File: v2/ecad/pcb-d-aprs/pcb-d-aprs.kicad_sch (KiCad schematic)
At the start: 96 parts, among them Q1 BC847 (PTT2, spare), Q2 BC847 (PTT to the module), Q3 2N7002 (EMCON inhibit in Q2 e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, Q4 BC857 (TR mirror from RADIO_P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, U1 TPS61089 boost 7.6 V / 2 A, U2 DNP bench: DMR858M 5 W UHF mo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, U3 AP2112K-3.3 digital, U4 AP2112K-3.3 analog, U5 STM32F302CBT6 128 KB (AIOC fi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, U6 USBLC6-2SC6, Y1 8MHz 20pF 5032

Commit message: feat(pcb-a,pcb-d): A20 and D6 routed and finished on the laptop [MESHSAT-795]
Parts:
- removed C1, C2: 22p NP0, Capacitor_SMD:C_0603_1608Metric, symbol Device:C
- removed C11: 4.7n NP0, Capacitor_SMD:C_0603_1608Metric, symbol Device:C
- removed C12, C15, C16: 100n, Capacitor_SMD:C_0603_1608Metric, symbol Device:C
- removed C31, C4, C5, C6: 4.7u, Capacitor_SMD:C_0603_1608Metric, symbol Device:C
- removed D2: red, LED_SMD:LED_0603_1608Metric, symbol Device:LED
- removed FB2: 600R@100MHz, Inductor_SMD:L_0603_1608Metric, symbol Device:FerriteBead
- removed J_SWD1: SWD/DFU 1.27 mm: BOOT0 SWO NRST SWDIO GND SWCLK 3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, Connector_PinHeader_1.27mm:PinHeader_1x07_P1.27mm_Vertical, symbol Connector_Generic:Conn_01x07
- removed R1, R18, R19: 1.5k, Resistor_SMD:R_0603_1608Metric, symbol Device:R
- removed R14, R16, R5: 5.1k, Resistor_SMD:R_0603_1608Metric, symbol Device:R
- removed R17: 100R, Resistor_SMD:R_0603_1608Metric, symbol Device:R
- removed R22: DNP 100R (mirror now via Q4), Resistor_SMD:R_0603_1608Metric, symbol Device:R
- removed U3: AP2112K-3.3 digital, Package_TO_SOT_SMD:SOT-23-5, symbol Regulator_Linear:AP2112K-3.3
- removed U4: AP2112K-3.3 analog, Package_TO_SOT_SMD:SOT-23-5, symbol Regulator_Linear:AP2112K-3.3
- removed U5: STM32F302CBT6 128 KB (AIOC firmware 1.4.1 is 128,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, Package_QFP:LQFP-48_7x7mm_P0.5mm, symbol MCU_ST_STM32F3:STM32F302CBTx
- removed U6: USBLC6-2SC6, Package_TO_SOT_SMD:SOT-23-6, symbol Power_Protection:USBLC6-2SC6
- removed Y1: 8MHz 20pF 5032, Crystal:Crystal_SMD_5032-2Pin_5.0x3.2mm, symbol Device:Crystal
- added C33, C35, C36, C38, C39: 100n, Capacitor_SMD:C_0603_1608Metric, symbol Device:C
- added C34: 10u, Capacitor_SMD:C_1210_3225Metric, symbol Device:C
- added C37: 4.7u, Capacitor_SMD:C_0603_1608Metric, symbol Device:C
- added J_UART1: DMR858M host-upgrade UART (bench, 3.3 V, 100R in 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, Connector_PinHeader_2.54mm:PinHeader_1x03_P2.54mm_Vertical, symbol Connector_Generic:Conn_01x03
- added TP13: MCLK, TestPoint:TestPoint_Pad_D1.5mm, symbol Connector:TestPoint
- added TP14: +3V3_AB, TestPoint:TestPoint_Pad_D1.5mm, symbol Connector:TestPoint
- added TP15: I2S_BCLK, TestPoint:TestPoint_Pad_D1.5mm, symbol Connector:TestPoint
- added U5: WM8960 audio codec QFN-32 (pins per datasheet tab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, Package_DFN_QFN:QFN-32-1EP_5x5mm_P0.5mm_EP3.1x3.1mm, symbol Connector_Generic:Conn_02x17_Odd_Even
- added U7: PCA9536 4-bit I2C expander 0x41: 0 PTT, 1 PTT2 (s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, Package_SO:SOIC-8_3.9x4.9mm_P1.27mm, symbol Interface_Expansion:PCA9536D
- added X1: 24 MHz 3.3 V oscillator 3225 (ASE-24.000MHZ-LC-T 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, Oscillator:Oscillator_SMD_Abracon_ASE-4Pin_3.2x2.5mm, symbol Oscillator:ASE-xxxMHz
- D1: value green -> green status (U7 bit 3 sinks)
- J_HARN1: value harness to PCB-A J_MEZZ1 (IDC 2x8); UART pair and PCB-A 3V3 unused -> harness to PCB-A J_MEZZ1 (IDC 2x8): I2S, I2C, the gated 3.3 V from B13, PTT lines
- R15: value 100R -> 1k
- R3: value 100R -> 100k
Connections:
- net ADC_BIAS is gone; now on net GND: R3.2
- net BIAS_NODE is gone; now on net SPKEN: R3.1
- net LDO_A is gone; now on net +3V3_AB: FB1.1
- net LED_R is gone; now on net LED_A: R15.2
- net +3.3VA: now also C33.1, C34.1, U5.21 (Pin_21), U5.26 (Pin_26), U5.32 (Pin_32)
- net +3V3: now also J_HARN1.12 (Pin_12); no longer C18.1, C7.1, C8.1
- net AFOUT: now also U5.31 (Pin_31)
- net GND: now also J_HARN1.8 (Pin_8), C33.2, C34.2, C35.2, C36.2, C37.2, C38.2, C39.2, J_UART1.1 (Pin_1), U5.20 (Pin_20), U5.24 (Pin_24), U5.28 (Pin_28), U5.33 (Pin_33), U5.9 (Pin_9), U7.4 (VSS), X1.2 (GND); no longer J_HARN1.9 (Pin_9)
- net LED_K: now also U7.7 (SDA); no longer R15.1
- net OUT1: now also U7.1 (IO0)
- net OUT2: now also U7.2 (IO1)
- net SPKEN: now also U7.3 (IO2); no longer J_HARN1.14 (Pin_14)
- net I2S_DOUT: now reaches J_HARN1.6 (Pin_6)
- net I2S_DOUT: now also U5.14 (Pin_14)
- net I2S_DIN: now reaches J_HARN1.7 (Pin_7)
- net I2S_DIN: now also U5.16 (Pin_16)
- net +5V_USB renamed +3V3_AB
- net +3V3_AB: now also C18.1, C7.1, C8.1, R15.1, C35.1, C36.1, C38.1, C39.1, TP14.1, U5.10 (Pin_10), U5.8 (Pin_8), U7.8 (VDD), X1.1 (EN), X1.4 (Vdd)
- net SPK_NODE renamed SPK_IN
- net SPK_IN: now also U5.4 (Pin_4)
- net USART_RX renamed UART_RX_H
- net UART_RX_H: now also J_UART1.2 (Pin_2)
- net USART_TX renamed UART_TX_H
- net UART_TX_H: now also J_UART1.3 (Pin_3)
- net USB_DM renamed I2S_LRCLK
- net I2S_LRCLK: now also U5.13 (Pin_13), U5.15 (Pin_15)
- net USB_DP renamed I2S_BCLK
- net I2S_BCLK: now also TP15.1, U5.12 (Pin_12)
- new net MCLK: TP13.1, U5.11 (Pin_11), X1.3 (OUT)
- new net SCL: J_HARN1.14 (Pin_14), U5.17 (Pin_17), U7.6 (SCL)
- new net SDA: J_HARN1.9 (Pin_9), U5.18 (Pin_18), U7.5 (IO3)
- new net VMID: C37.1, U5.27 (Pin_27)
- no-connect marks 30 -> 20
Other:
- note added: "AUDIO PATHS, PTT + TR MIRROR, UART, LED"
- note added: "D6 CORE: RAILS, WM8960 CODEC ON I2S + I2C, 24 MHz CLOCK, PCA9536 PTT EXPANDER, UART HEADER"
- note removed: "AIOC-DERIVED CORE: LDOs, STM32F302C8, CLOCK, SWD/DFU"
- note removed: "USB, AUDIO PATHS, PTT + TR MIRROR, UART, LEDS"

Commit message: feat(pcb-d): D7 routed and finished for the DMR858M V1.0 board [MESHSAT-804]
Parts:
- removed JP1: channel bit CH8 to GND (open = default), Jumper:SolderJumper-2_P1.3mm_Open_RoundedPad1.0x1.5mm, symbol Jumper:SolderJumper_2_Open
- removed JP2: channel bit CH4 to GND (open = default), Jumper:SolderJumper-2_P1.3mm_Open_RoundedPad1.0x1.5mm, symbol Jumper:SolderJumper_2_Open
- removed JP3: channel bit CH2 to GND (open = default), Jumper:SolderJumper-2_P1.3mm_Open_RoundedPad1.0x1.5mm, symbol Jumper:SolderJumper_2_Open
- removed JP4: channel bit CH1 to GND (open = default), Jumper:SolderJumper-2_P1.3mm_Open_RoundedPad1.0x1.5mm, symbol Jumper:SolderJumper_2_Open
- removed JP5: CS to GND = module sleep, Jumper:SolderJumper-2_P1.3mm_Open_RoundedPad1.0x1.5mm, symbol Jumper:SolderJumper_2_Open
- removed J_UART1: DMR858M host-upgrade UART (bench, 3.3 V, 100R in 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, Connector_PinHeader_2.54mm:PinHeader_1x03_P2.54mm_Vertical, symbol Connector_Generic:Conn_01x03
- removed U7: PCA9536 4-bit I2C expander 0x41: 0 PTT, 1 PTT2 (s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, Package_SO:SOIC-8_3.9x4.9mm_P1.27mm, symbol Interface_Expansion:PCA9536D
- added C40: 100n, Capacitor_SMD:C_0603_1608Metric, symbol Device:C
- added R42, R43, R44, R45, R46, R48: 1k, Resistor_SMD:R_0603_1608Metric, symbol Device:R
- added R47: 10k, Resistor_SMD:R_0603_1608Metric, symbol Device:R
- added R49, R50, R51, R52: 100k, Resistor_SMD:R_0603_1608Metric, symbol Device:R
- added U7: PCA9555PW 0x26: PTT, PTT2, LED, CS, COS in, chann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, Package_SO:TSSOP-24_4.4x7.8mm_P0.65mm, symbol Interface_Expansion:PCA9555PW
- added U8: SC16IS740IPW I2C-to-UART bridge 0x48, 24 MHz exte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, Package_SO:TSSOP-16_4.4x5mm_P0.65mm, symbol Connector_Generic:Conn_01x16
- R2: value 4.7k -> 47k
- R4: value 1.5k -> 1k
- TP6: value SPKEN -> RADIO_COS
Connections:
- net +3V3: no longer R36.2
- net +3V3_AB: now also R36.2, C40.1, R47.2, U7.2 (A1), U7.24 (VDD), U7.3 (A2), U8.1 (Pin_1), U8.2 (Pin_2), U8.3 (Pin_3), U8.8 (Pin_8)
- net CH1: now also R46.1
- net CH2: now also R45.1
- net CH4: now also R44.1
- net CH8: now also R43.1
- net CS: now also R48.2
- net GND: now also C40.2, R49.2, R50.2, R51.2, R52.2, U7.12 (VSS), U7.21 (A0), U8.11 (Pin_11), U8.9 (Pin_9)
- net LED_K: now also U7.6 (IO0_2)
- net MCLK: now also U8.15 (Pin_15)
- net OUT1: now also U7.4 (IO0_0)
- net OUT2: now also U7.5 (IO0_1)
- net SCL: now also U7.22 (SCL), U8.5 (Pin_5)
- net SDA: now also U7.23 (SDA), U8.6 (Pin_6)
- net SPKEN renamed RADIO_COS
- net RADIO_COS: now also R42.1
- net UART_RX_H renamed BR_RX
- net BR_RX: now also U8.13 (Pin_13)
- net UART_TX_H renamed BR_TX
- net BR_TX: now also U8.12 (Pin_12)
- new net BR_nRST: R47.1, U8.14 (Pin_14)
- new net CH1_IN: R46.2, R52.1, U7.13 (IO1_0)
- new net CH2_IN: R45.2, R51.1, U7.11 (IO0_7)
- new net CH4_IN: R44.2, R50.1, U7.10 (IO0_6)
- new net CH8_IN: R43.2, R49.1, U7.9 (IO0_5)
- new net CS_CTL: R48.1, U7.7 (IO0_3)
- new net RADIO_COS_IN: R42.2, U7.8 (IO0_4)
- no-connect marks 20 -> 32
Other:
- note added: "AUDIO PATHS, PTT + TR MIRROR, BRIDGE UART LINES, LED"
- note added: "D7 CORE: RAILS, WM8960 CODEC ON I2S + I2C, 24 MHz CLOCK, PCA9555 EXPANDER 0x26, SC16IS740 UART BRIDGE 0x48"
- note added: "DMR858M RADIO MODULE (V1.0 BOARD): CS PULL-UP AND CONTROL, KNOB CODE AND COS INTO THE EXPANDER"
- note removed: "AUDIO PATHS, PTT + TR MIRROR, UART, LED"
- note removed: "D6 CORE: RAILS, WM8960 CODEC ON I2S + I2C, 24 MHz CLOCK, PCA9536 PTT EXPANDER, UART HEADER"
- note removed: "DMR858M RADIO MODULE: CHANNEL JUMPERS, CS"

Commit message: feat(ecad): D8 routed clean and released (SA868 exciter, T/R relay, LPF, USB audio and control set), C7 generators (backer ring, RP2040 panel controller, PDi e-paper driver, Xenarc face, headset jacks), per-closure stub acceptance, plane-net fanout fixes [MESHSAT-830]
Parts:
- removed D1: green status (U7 bit 3 sinks), LED_SMD:LED_0603_1608Metric, symbol Device:LED
- removed Q1: BC847 (PTT2, spare), Package_TO_SOT_SMD:SOT-23, symbol Transistor_BJT:BC847
- removed Q2: BC847 (PTT to the module), Package_TO_SOT_SMD:SOT-23, symbol Transistor_BJT:BC847
- removed Q4: BC857 (TR mirror from RADIO_PTT), Package_TO_SOT_SMD:SOT-23, symbol Transistor_BJT:BC857
- removed U1: TPS61089 boost 7.6 V / 2 A, Package_DFN_QFN:Texas_VQFN-RNR0011A-11, symbol Regulator_Switching:TPS61089
- removed U2: DNP bench: DMR858M 5 W UHF module on 2 x 1x12 2.5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, meshsat:DMR858M, symbol Connector_Generic:Conn_02x12_Odd_Even
- removed U5: WM8960 audio codec QFN-32 (pins per datasheet tab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, Package_DFN_QFN:QFN-32-1EP_5x5mm_P0.5mm_EP3.1x3.1mm, symbol Connector_Generic:Conn_02x17_Odd_Even
- removed U7: PCA9555PW 0x26: PTT, PTT2, LED, CS, COS in, chann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, Package_SO:TSSOP-24_4.4x7.8mm_P0.65mm, symbol Interface_Expansion:PCA9555PW
- removed U8: SC16IS740IPW I2C-to-UART bridge 0x48, 24 MHz exte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, Package_SO:TSSOP-16_4.4x5mm_P0.65mm, symbol Connector_Generic:Conn_01x16
- removed X1: 24 MHz 3.3 V oscillator 3225 (ASE-24.000MHZ-LC-T 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, Oscillator:Oscillator_SMD_Abracon_ASE-4Pin_3.2x2.5mm, symbol Oscillator:ASE-xxxMHz
- added C1, C2, C5: 47u 6.3V X5R 1210, Capacitor_SMD:C_1210_3225Metric, symbol Device:C
- added C11, C15, C16, C4, C49, C50, C51, C52, C53, C54, C55, C56, C57, C6, C62, C63: 100n, Capacitor_SMD:C_0603_1608Metric, symbol Device:C
- added C12, C19, C31, C41, C42, C46, C47, C48: 1u, Capacitor_SMD:C_0603_1608Metric, symbol Device:C
- added C3: 10u, Capacitor_SMD:C_0805_2012Metric, symbol Device:C
- added C43: 100p NP0, Capacitor_SMD:C_0402_1005Metric, symbol Device:C
- added C44, C45: 1n NP0, Capacitor_SMD:C_0402_1005Metric, symbol Device:C
- added C58, C60: 22p 500V NP0 1206, Capacitor_SMD:C_1206_3216Metric, symbol Device:C
- added C59: 39p 500V NP0 1206, Capacitor_SMD:C_1206_3216Metric, symbol Device:C
- added C61: 4.7n, Capacitor_SMD:C_0402_1005Metric, symbol Device:C
- added D1: SMBJ5.0A, Diode_SMD:D_SMB, symbol Device:D_TVS
- added D2: 1N4148W coil flyback, Diode_SMD:D_SOD-123, symbol Diode:1N4148W
- added JP1: electret bias headset 1 (close for an electret mi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, Jumper:SolderJumper-2_P1.3mm_Open_RoundedPad1.0x1.5mm, symbol Jumper:SolderJumper_2_Open
- added JP2: electret bias headset 2, Jumper:SolderJumper-2_P1.3mm_Open_RoundedPad1.0x1.5mm, symbol Jumper:SolderJumper_2_Open
- added J_ANT: antenna (SMA, pigtail to A22's VHF jack J_RF1), Connector_Coaxial:SMA_Amphenol_132134_Vertical, symbol Connector:Conn_Coaxial
- added J_HS1: headset 1 lead (JST-PH 1x5 to the face plate U-17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, Connector_JST:JST_PH_B5B-PH-K_1x05_P2.00mm_Vertical, symbol Connector_Generic:Conn_01x05
- added J_HS2: headset 2 lead (JST-PH 1x5 to the face plate U-17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, Connector_JST:JST_PH_B5B-PH-K_1x05_P2.00mm_Vertical, symbol Connector_Generic:Conn_01x05
- added J_PAIN: PA drive (U.FL, coax to the RA30H1317M1 input on 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, Connector_Coaxial:U.FL_Hirose_U.FL-R-SMT-1_Vertical, symbol Connector:Conn_Coaxial
- added J_PAOUT: PA output (SMA, coax from the RA30H1317M1 output 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, Connector_Coaxial:SMA_Amphenol_132134_Vertical, symbol Connector:Conn_Coaxial
- added J_USB3: spare hub port 3 (JST-PH 1x4): 5V D- D+ GND, Connector_JST:JST_PH_B4B-PH-K_1x04_P2.00mm_Vertical, symbol Connector_Generic:Conn_01x04
- added J_VGG: PA gate bias lead (JST-PH 1x2 to the RA30H1317M1 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, Connector_JST:JST_PH_B2B-PH-K_1x02_P2.00mm_Vertical, symbol Connector_Generic:Conn_01x02
- added K1: Omron G6K-2F-Y 5 VDC DPDT signal relay, T/R, Relay_SMD:Relay_DPDT_Omron_G6K-2F-Y, symbol Relay:G6K-2
- added L2: 68nH 1812 (LPF), Inductor_SMD:L_1812_4532Metric, symbol Device:L
- added LED1: green power, LED_SMD:LED_0603_1608Metric, symbol Device:LED
- added LED2: amber record, LED_SMD:LED_0603_1608Metric, symbol Device:LED
- added LED3: green playback, LED_SMD:LED_0603_1608Metric, symbol Device:LED
- added LED4: red transmit, LED_SMD:LED_0603_1608Metric, symbol Device:LED
- added LED5: amber PA keyed, LED_SMD:LED_0603_1608Metric, symbol Device:LED
- added LED6: green receive (AUDIO_ON low), LED_SMD:LED_0603_1608Metric, symbol Device:LED
- added Q1: 2N7002 PA_EN -> H/L low (never tie H/L high), Package_TO_SOT_SMD:SOT-23, symbol Transistor_FET:2N7002
- added Q2: 2N7002 relay coil, Package_TO_SOT_SMD:SOT-23, symbol Transistor_FET:2N7002
- added Q4, Q5, Q6, Q7, Q8, Q9: 2N7002, Package_TO_SOT_SMD:SOT-23, symbol Transistor_FET:2N7002
- added R1: 2.2k, Resistor_SMD:R_0603_1608Metric, symbol Device:R
- added R14, R18, R19, R22, R23, R24, R25: 15k, Resistor_SMD:R_0603_1608Metric, symbol Device:R
- added R16, R17, R20, R21, R6, R7: 22, Resistor_SMD:R_0603_1608Metric, symbol Device:R
- added R26, R27: 33, Resistor_SMD:R_0603_1608Metric, symbol Device:R
- added R28: 1.5k, Resistor_SMD:R_0603_1608Metric, symbol Device:R
- added R29: 1k, Resistor_SMD:R_0603_1608Metric, symbol Device:R
- added R5, R66, R67, R68, R69, R70, R71, R72, R73, R74, R75, R76, R77, R78, R79: 10k, Resistor_SMD:R_0603_1608Metric, symbol Device:R
- added R53: 100k, Resistor_SMD:R_0603_1608Metric, symbol Device:R
- added R54, R56: 27 1% 2010, Resistor_SMD:R_2010_5025Metric, symbol Device:R
- added R55: 36 1% 2010, Resistor_SMD:R_2010_5025Metric, symbol Device:R
- added TP16: PA_EN, TestPoint:TestPoint_Pad_D1.5mm, symbol Connector:TestPoint
- added TP17: EXP_SPARE1, TestPoint:TestPoint_Pad_D1.5mm, symbol Connector:TestPoint
- added TP18: EXP_SPARE2, TestPoint:TestPoint_Pad_D1.5mm, symbol Connector:TestPoint
- added TP19: EXP_SPARE3, TestPoint:TestPoint_Pad_D1.5mm, symbol Connector:TestPoint
- added TP20: EXP_SPARE4, TestPoint:TestPoint_Pad_D1.5mm, symbol Connector:TestPoint
- added TP21: EXP_SPARE5, TestPoint:TestPoint_Pad_D1.5mm, symbol Connector:TestPoint
- added TP22: EXP_SPARE6, TestPoint:TestPoint_Pad_D1.5mm, symbol Connector:TestPoint
- added TP23: EXP_SPARE7, TestPoint:TestPoint_Pad_D1.5mm, symbol Connector:TestPoint
- added TP24: EXP_SPARE8, TestPoint:TestPoint_Pad_D1.5mm, symbol Connector:TestPoint
- added U1: TLV75533PDBV 3.3 V 500 mA LDO (1 IN 2 GND 3 EN 4 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, Package_TO_SOT_SMD:SOT-23-5, symbol Connector_Generic:Conn_01x05
- added U10: 74LVC1G08 AND: headsets AND software PTT (RTS), Package_TO_SOT_SMD:SOT-23-5, symbol Connector_Generic:Conn_01x05
- added U11: 74LVC1G04 inverter (2 A 4 Y): PTT_ANY, Package_TO_SOT_SMD:SOT-23-5, symbol Connector_Generic:Conn_01x05
- added U12: 74LVC1G08 AND: KEY = PTT_ANY AND TX_INHIBIT_n (th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, Package_TO_SOT_SMD:SOT-23-5, symbol Connector_Generic:Conn_01x05
- added U13: 74LVC1G04 inverter: KEY -> SA868 PTT (low = trans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, Package_TO_SOT_SMD:SOT-23-5, symbol Connector_Generic:Conn_01x05
- added U14: 74LVC1G08 AND: PA_KEY = KEY AND PA_EN (A22's PA r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, Package_TO_SOT_SMD:SOT-23-5, symbol Connector_Generic:Conn_01x05
- added U15: TPS22810DRV, Package_SON:WSON-6-1EP_2x2mm_P0.65mm_EP1x1.6mm, symbol Power_Management:TPS22810DRV
- added U16: PCA9555PW 0x26: COS, PTT states, KEY, PA_KEY in; 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, Package_SO:TSSOP-24_4.4x7.8mm_P0.65mm, symbol Interface_Expansion:PCA9555PW
- added U2: NiceRF SA868 VHF 2 W exciter, bench-fitted (caste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, meshsat:NiceRF_SA868, symbol Connector_Generic:SA868
- added U3: CP2102N-A02-GQFN28 USB-UART bridge (SAU), Package_DFN_QFN:QFN-28-1EP_5x5mm_P0.5mm_EP3.35x3.35mm, symbol Connector_Generic:CP2102N
- added U4: TUSB2046BI four-port USB 2.0 full-speed hub (LQFP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, Package_QFP:LQFP-32_7x7mm_P0.8mm, symbol Connector_Generic:TUSB2046B
- added U5: USBLC6-2SC6, Package_TO_SOT_SMD:SOT-23-6, symbol Power_Protection:USBLC6-2SC6
- added U6: TI PCM2912A USB audio codec (TQFP-32): mono input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, Package_QFP:TQFP-32_7x7mm_P0.8mm, symbol Connector_Generic:PCM2912A
- added U7: TI TPA6132A2 headphone amplifier (QFN-16), receiv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, Package_DFN_QFN:QFN-16-1EP_3x3mm_P0.5mm_EP1.75x1.75mm, symbol Connector_Generic:TPA6132A2
- added U8: TLV9062IDGK dual op amp (1 OUT1 2 IN1- 3 IN1+ 4 V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, Package_SO:VSSOP-8_3x3mm_P0.65mm, symbol Connector_Generic:Conn_01x08
- added U9: 74LVC1G08 AND (1 A 2 B 3 GND 4 Y 5 VCC): both hea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, Package_TO_SOT_SMD:SOT-23-5, symbol Connector_Generic:Conn_01x05
- added Y1: 6 MHz 3225 (CL 20 pF; C1 = C2 = 27 pF and Rd 1.5k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, Crystal:Crystal_SMD_3225-4Pin_3.2x2.5mm, symbol Device:Crystal_GND24
- added Y2: 6 MHz 3225 (codec clock; 18 pF loads, to confirm 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, Crystal:Crystal_SMD_3225-4Pin_3.2x2.5mm, symbol Device:Crystal_GND24
- C10: footprint Capacitor_SMD:C_0603_1608Metric -> Capacitor_SMD:C_0805_2012Metric
- C13, C14: value 4.7u -> 27p NP0; footprint Capacitor_SMD:C_0603_1608Metric -> Capacitor_SMD:C_0402_1005Metric
- C17, C25, C33, C40, C9: value 100n -> 10u; footprint Capacitor_SMD:C_0603_1608Metric -> Capacitor_SMD:C_0805_2012Metric
- C18, C32, C35, C36, C38, C8: value 100n -> 1u
- C20, C30: value 100n 25V -> 1u
- C22: value 4.7n -> 1u
- C23: value 22u 10V X7R 1210 -> 1u; footprint Capacitor_SMD:C_1210_3225Metric -> Capacitor_SMD:C_0603_1608Metric
- C24: value 22u 10V X7R 1210 -> 10u; footprint Capacitor_SMD:C_1210_3225Metric -> Capacitor_SMD:C_0805_2012Metric
- C26, C27: value 22u 25V X7R 1210 -> 18p NP0; footprint Capacitor_SMD:C_1210_3225Metric -> Capacitor_SMD:C_0402_1005Metric
- C28, C29: value 22u 25V X7R 1210 -> 1u; footprint Capacitor_SMD:C_1210_3225Metric -> Capacitor_SMD:C_0603_1608Metric
- C34: value 10u -> 1u; footprint Capacitor_SMD:C_1210_3225Metric -> Capacitor_SMD:C_0603_1608Metric
- C37, C7: value 4.7u -> 1u
- FB1: value 600R@100MHz -> 600R 2A ferrite (the exciter's 1 A transmit pulses); footprint Inductor_SMD:L_0603_1608Metric -> Inductor_SMD:L_0805_2012Metric
- J_HARN1: value harness to PCB-A J_MEZZ1 (IDC 2x8): I2S, I2C, the gated 3.3 V from B13, PTT lines -> A22 mezzanine harness J_MEZZ1 (IDC 2x8): USB pair, PTT mirror, inhibit, PA rail state, I2C, 3.3 V
- J_PWR1: value cell node from PCB-A J_MEZZ_PWR (JST-VH) -> 5 V from A22 J_MEZZ_PWR1 (JST-VH, 2 A eFuse on A22): + -
- L1: value 1.5uH XAL6030-152MEB (Isat 12 A, 5.6 mOhm) -> 68nH 1812 (LPF, 145 MHz 5th order; values to be verified in MESHSAT-818); footprint Inductor_SMD:L_Coilcraft_XAL6030-XXX -> Inductor_SMD:L_1812_4532Metric
- Q3: value 2N7002 (EMCON inhibit in Q2 emitter) -> 2N7002; LCSC (none) -> C8545
- R10: value 1.5k -> 10k
- R12, R13: value 22R -> 22
- R15: value 1k -> 15k
- R2: value 47k -> 100k
- R30: value 301k 1% (500 kHz) -> 1k
- R31: value 100k 1% (ILIM 10 A peak, 9 A min) -> 10k
- R32: value 17.4k -> 10k
- R33: value 105k 1% -> 4.7k
- R34: value 20k 1% -> 100k
- R35, R38, R39: value 100k -> 10k
- R37, R45, R46: value 1k -> 10k
- R40: value 10k -> 4.7k
- R41: value 100R -> 4.7k
- R42: value 1k -> 220k
- R43, R44: value 1k -> 2.2k
- R48: value 1k -> 100
- R49, R50, R52: value 100k -> 1k
- R51: value 100k -> 2.2k
- R8: value 100R -> 1.5k
- R9: value 100R -> 10k
- TP1: value V8 -> AF_OUT
- TP10: value RADIO_PTT2 -> AB_SPARE
- TP11: value MEZZ_EN -> SA_TXD
- TP12: value TX_INHIBIT_n -> SA_RXD
- TP13: value MCLK -> PTT_SW_n
- TP14: value +3V3_AB -> SA_PD
- TP15: value I2S_BCLK -> TX_INHIBIT_n
- TP2: value GND -> MIC_SUM
- TP3: value RADIO_PTT -> KEY
- TP4: value RADIO_MIC -> PA_KEY
- TP5: value RADIO_SPK -> +3V3_D8
- TP6: value RADIO_COS -> +5V_D8
- TP7: value +3V3 -> VGG_SW
- TP8: value VIN_CELL -> RX_MIX
- TP9: value TR_APRS -> ZEROIZE_HW
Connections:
- net AFOUT is gone; now on net TX_INHIBIT_n: R2.1
- net CS_CTL is gone; now on net KEY: R48.1
- net FSW is gone; now on net +3V3_D8: R30.1
- net I2S_DOUT is gone; now on net TX_INHIBIT_n: J_HARN1.6 (Pin_6)
- net I2S_LRCLK is gone; now on net GND: J_HARN1.4 (Pin_4)
- net LED_A is gone; now on net GND: R15.2
- net Q1_B is gone; now on net +3V3_D8: R10.2
- net RADIO_COS_IN is gone; now on net MICAMP_IN_N: R42.2
- net RADIO_RX is gone; now on net +3V3_D8: R8.2
- net SPK_IN is gone; now on net GND: C14.2
- net +3V3: now also C63.1, R67.2, R69.2, R71.2, R73.2, R75.2, R77.2, R79.2, U16.2 (A1), U16.24 (VDD), U16.3 (A2); no longer C17.1, R38.2, R39.2, TP7.1
- net GND: now also C13.2, C20.2, R2.2, R32.2, R37.2, R39.2, R47.2, C1.2, C11.2, C12.2, C15.2, C16.2, C19.2, C2.2, C3.2, C31.2, C4.2, C44.2, C45.2, C49.2, C5.2, C50.2, C51.2, C52.2, C53.2, C54.2, C55.2, C56.2, C57.2, C58.2, C59.2, C6.2, C60.2, C61.2, C62.2, C63.2, D1.1 (A1), J_ANT.2 (Ext), J_HS1.2 (Pin_2), J_HS1.4 (Pin_4), J_HS2.2 (Pin_2), J_HS2.4 (Pin_4), J_PAIN.2 (Ext), J_PAOUT.2 (Ext), J_USB3.4 (Pin_4), J_VGG.2 (Pin_2), LED1.1 (K), LED4.1 (K), LED5.1 (K), Q1.2 (S), Q2.2 (S), R14.2, R18.2, R19.2, R22.2, R23.2, R24.2, R25.2, R53.2, R55.2, U1.2 (Pin_2), U10.3 (Pin_3), U11.3 (Pin_3), U12.3 (Pin_3), U13.3 (Pin_3), U14.3 (Pin_3), U15.4 (GND), U15.7 (GND), U16.12 (VSS), U16.21 (A0), U2.10 (GND), U2.9 (GND), U3.29 (GND), U3.3 (GND), U4.27 (TSTPLL/48MCLK), U4.28 (GND), U4.31 (TSTMODE), U4.7 (GND), U4.8 (BUSPWR), U5.2 (GND), U6.1 (BGND), U6.13 (AGND), U6.20 (HGND), U6.23 (MAMP), U6.24 (POWER), U6.25 (PGND), U6.28 (TEST0), U6.6 (DGND), U7.10 (PGND), U7.15 (SGND), U7.17 (PAD), U7.7 (G1), U8.4 (Pin_4), U9.3 (Pin_3), Y1.2 (G), Y1.4 (G), Y2.2 (G), Y2.4 (G); no longer C28.2, C30.2, C34.2, C35.2, C36.2, J_HARN1.5 (Pin_5), Q3.2 (S), R31.2, R35.2, R4.2, R49.2, R50.2, R51.2, R52.2, TP2.1
- net SCL: now also J_HARN1.10 (Pin_10), U16.22 (SCL); no longer J_HARN1.14 (Pin_14)
- net SDA: now also U16.23 (SDA)
- net TR_APRS: now also J_HARN1.5 (Pin_5), R48.2; no longer J_HARN1.10 (Pin_10), R41.2, TP9.1
- net TX_INHIBIT_n: now also TP15.1, U12.2 (Pin_2); no longer J_HARN1.15 (Pin_15), R37.1, R38.1, TP12.1
- removed net +3.3VA: C10.1, C33.1, C34.1, C9.1, FB1.2
- removed net +3V3_AB: C18.1, C35.1, C36.1, C38.1, C39.1, C40.1, C7.1, C8.1, FB1.1, J_HARN1.2 (Pin_2), R15.1, R36.2, R47.2, TP14.1
- net BOOT renamed PCM_VCCA
- net PCM_VCCA: now also U6.15 (VCCA)
- net BR_RX renamed +3V3_D8
- net +3V3_D8: now also C17.1, C8.1, C9.1, Q3.1 (G), R51.1, TP5.1, C15.1, C16.1, C51.1, C52.1, C53.1, C54.1, C55.1, C56.1, Q4.1 (G), Q5.1 (G), Q6.1 (G), Q7.1 (G), Q8.1 (G), Q9.1 (G), R1.1, R29.1, R5.2, R66.2, R68.2, R70.2, R72.2, R74.2, R76.2, R78.2, U1.5 (Pin_5), U10.5 (Pin_5), U11.5 (Pin_5), U12.5 (Pin_5), U13.5 (Pin_5), U14.5 (Pin_5), U4.25 (VCC), U4.26 (EXTMEM), U4.3 (VCC), U4.6 (EEDATA/GANGED), U7.6 (G0), U9.5 (Pin_5)
- net BR_TX renamed HUB_DP0
- net HUB_DP0: now also R6.2, U4.1 (DP0)
- net BR_nRST renamed MIC_SUM
- net MIC_SUM: now also R45.2, R46.2, TP2.1, C48.1
- net BST_VCC renamed PCM_VCCL
- net PCM_VCCL: now also U6.19 (VCCL)
- net CH1 renamed PCM_R_AC
- net PCM_R_AC: now also C47.2
- net CH1_IN renamed PA_KEY
- net PA_KEY: now also R50.1, TP4.1, Q7.2 (S), R74.1, U14.4 (Pin_4), U15.5 (EN/UVLO); no longer R46.2
- net CH2 renamed MICAMP_AC
- net MICAMP_AC: now also C46.2
- removed net CH2_IN: R45.2, R51.1
- net CH4 renamed HS2_BIAS_R
- net HS2_BIAS_R: now also JP2.2 (B)
- net CH4_IN renamed +5V_D8
- net +5V_D8: now also C18.1, C32.1, C33.1, C39.1, C7.1, FB1.1, J_PWR1.1 (Pin_1), R38.1, R43.2, TP6.1, C1.1, C2.1, C3.1, C4.1, C57.1, D1.2 (A2), D2.1 (K), J_USB3.1 (Pin_1), K1.1, U1.1 (Pin_1), U1.3 (Pin_3), U15.6 (VIN), U3.7 (VREGIN), U3.8 (VBUS), U5.5 (VBUS), U6.2 (VBUS), U7.14 (VDD), U8.8 (Pin_8); no longer R50.1
- net CH8 renamed HS1_BIAS_R
- net HS1_BIAS_R: now also JP1.2 (B)
- net CH8_IN renamed KEY
- net KEY: now also TP3.1, Q6.2 (S), R72.1, U12.4 (Pin_4), U13.2 (Pin_2), U14.1 (Pin_1); no longer R43.2
- net COMP renamed AF_DIV
- net AF_DIV: now also C28.1, R31.2
- net COMPC renamed PCM_VCCR
- net PCM_VCCR: now also U6.21 (VCCR); no longer R32.2
- net CS renamed PCM_L_AC
- net PCM_L_AC: now also C34.2; no longer R48.2
- net FB8 renamed MMUTE
- net MMUTE: now also U6.30 (MMUTE)
- net I2S_BCLK renamed USB_D8_N
- net USB_D8_N: now also R7.1, U5.3 (I/O2), U5.4 (I/O2); no longer TP15.1
- net I2S_DIN renamed PA_EN
- net PA_EN: now also R3.1, Q1.1 (G), TP16.1, U14.2 (Pin_2)
- net ILIM renamed AF_OUT
- net AF_OUT: now also R35.1, TP1.1, U2.3 (AF_OUT)
- net MCLK renamed PTT_SW_n
- net PTT_SW_n: now also R5.1, U10.2 (Pin_2), U3.24 (RTS)
- removed net MEZZ_EN: J_HARN1.11 (Pin_11), R35.1, TP11.1
- removed net MIC_NODE: C13.1, R2.2, R4.1
- net OUT1 renamed HUB_XTAL2R
- net HUB_XTAL2R: now also C14.1, Y1.3
- net OUT2 renamed HUB_RST_n
- net HUB_RST_n: now also C12.1, U4.4 (RESET_n)
- net Q1_C renamed HUB_DP1
- net HUB_DP1: now also U4.12 (DP1)
- net Q2_B renamed HUB_XTAL2
- net HUB_XTAL2: now also U4.29 (XTAL2)
- net Q2_C renamed HUB_DM1
- net HUB_DM1: now also U4.11 (DM1)
- net Q2_E renamed X_COS_n
- net X_COS_n: now also R67.1, U16.4 (IO0_0)
- removed net Q3_G: C32.1, Q3.1 (G), R37.2
- net Q4_B renamed MICAMP_IN_N
- net MICAMP_IN_N: now also R41.2, C43.2, U8.2 (Pin_2)
- net Q4_C renamed HS2_MIC_AC
- net HS2_MIC_AC: now also C42.2
- removed net RADIO_COS: R3.1, R42.1, TP6.1
- removed net RADIO_MIC: C13.2, TP4.1
- removed net RADIO_PTT: R13.2, R39.1, R40.1, TP3.1
- net RADIO_PTT2 renamed AB_SPARE
- net AB_SPARE: now also J_HARN1.15 (Pin_15); no longer R12.2
- removed net RADIO_SPK: C14.1, TP5.1
- net RADIO_TX renamed HUB_OVRCUR_n
- net HUB_OVRCUR_n: now also U4.10 (OVRCUR1_n), U4.14 (OVRCUR2_n), U4.18 (OVRCUR3_n), U4.22 (OVRCUR4_n)
- removed net SW: C20.2, L1.2, R30.2
- removed net V8: C26.1, C27.1, C28.1, C29.1, C30.1, R33.1, TP1.1
- removed net VIN_CELL: C23.1, C24.1, C25.1, J_PWR1.1 (Pin_1), L1.1, TP8.1
- net VMID renamed AMP_INL_N
- net AMP_INL_N: now also U7.1 (INL-)
- new net +5V_SA: C5.1, C6.1, FB1.2, U2.8 (VBAT)
- new net AMP_CPN: C30.2, U7.9 (CPN)
- new net AMP_CPP: C30.1, U7.11 (CPP)
- new net AMP_EN: Q9.2 (S), R78.1, U7.13 (EN)
- new net AMP_HPVDD: C31.1, U7.12 (HPVDD)
- new net AMP_HPVSS: C29.1, U7.8 (HPVSS)
- new net AMP_INL_P: C35.2, U7.2 (INL+)
- new net AMP_INR_N: C38.1, U7.4 (INR-)
- new net AMP_INR_P: C36.2, U7.3 (INR+)
- new net EXP_INT: J_HARN1.11 (Pin_11), U16.1 (~{INT})
- new net EXP_SPARE1: TP17.1, U16.13 (IO1_0)
- new net EXP_SPARE2: TP18.1, U16.14 (IO1_1)
- new net EXP_SPARE3: TP19.1, U16.15 (IO1_2)
- new net EXP_SPARE4: TP20.1, U16.16 (IO1_3)
- new net EXP_SPARE5: TP21.1, U16.17 (IO1_4)
- new net EXP_SPARE6: TP22.1, U16.18 (IO1_5)
- new net EXP_SPARE7: TP23.1, U16.19 (IO1_6)
- new net EXP_SPARE8: TP24.1, U16.20 (IO1_7)
- new net HS1_MIC: C41.1, C44.1, JP1.1 (A), J_HS1.3 (Pin_3)
- new net HS1_MIC_AC: C41.2, R40.1
- new net HS1_SPK: J_HS1.1 (Pin_1), U7.16 (OUTL)
- new net HS2_MIC: C42.1, C45.1, JP2.1 (A), J_HS2.3 (Pin_3)
- new net HS2_SPK: J_HS2.1 (Pin_1), U7.5 (OUTR)
- new net HUB_DM0: R7.2, U4.2 (DM0)
- new net HUB_DM2: R17.1, U4.15 (DM2)
- new net HUB_DM3: R21.1, U4.19 (DM3)
- new net HUB_DM4: R25.1, U4.23 (DM4)
- new net HUB_DP2: R16.1, U4.16 (DP2)
- new net HUB_DP3: R20.1, U4.20 (DP3)
- new net HUB_DP4: R24.1, U4.24 (DP4)
- new net HUB_XTAL1: C13.1, U4.30 (XTAL1), Y1.1
- new net LED_PA_A: LED5.2 (A), R50.2
- new net LED_PLAY_A: LED3.2 (A), R30.2
- new net LED_PLAY_K: LED3.1 (K), U6.32 (PLAY)
- new net LED_PWR_A: LED1.2 (A), R1.2
- new net LED_REC_A: LED2.2 (A), R29.2
- new net LED_REC_K: LED2.1 (K), U6.31 (REC)
- new net LED_RX_A: LED6.2 (A), R51.2
- new net LED_TX_A: LED4.2 (A), R49.2
- new net MICAMP_OUT: C43.1, C46.1, R42.1, U8.1 (Pin_1)
- new net MIC_IN: C48.2, U2.18 (MIC_IN)
- new net OPB_OUT: U8.6 (Pin_6), U8.7 (Pin_7)
- new net PCM_VCCP: C23.1, U6.26 (VCCP)
- new net PCM_VCOM1: C24.1, U6.11 (VCOM1)
- new net PCM_VCOM2: C25.1, U6.12 (VCOM2)
- new net PCM_VDD: C19.1, R28.2, U6.27 (TEST1), U6.5 (VDD)
- new net PCM_VIN: C28.2, U6.16 (VIN)
- new net PCM_VOUTL: C34.1, U6.18 (VOUTL)
- new net PCM_VOUTR: C47.1, U6.22 (VOUTR)
- new net PCM_XTI: C26.1, U6.8 (XTI), Y2.1
- new net PCM_XTO: C27.1, U6.7 (XTO), Y2.3
- new net PTT_ANY: U11.4 (Pin_4), U12.1 (Pin_1)
- new net PTT_ANY_n: U10.4 (Pin_4), U11.2 (Pin_2)
- new net PTT_HS1_n: C49.1, J_HS1.5 (Pin_5), Q4.2 (S), R68.1, U9.1 (Pin_1)
- new net PTT_HS2_n: C50.1, J_HS2.5 (Pin_5), Q5.2 (S), R70.1, U9.2 (Pin_2)
- new net PTT_HS_n: U10.1 (Pin_1), U9.4 (Pin_4)
- new net RF_ANT: J_ANT.1 (In), K1.6
- new net RF_DRV: J_PAIN.1 (In), R56.2
- new net RF_LPF_M: C59.1, L1.2, L2.1
- new net RF_LPF_OUT: C60.1, K1.5, L2.2
- new net RF_PAD_IN: K1.4, R54.1
- new net RF_PAD_M: R54.2, R55.1, R56.1
- new net RF_PAOUT: C58.1, J_PAOUT.1 (In), L1.1
- new net RF_RX: K1.2, K1.7
- new net RF_SA: K1.3, U2.12 (ANT)
- new net RLY_DRV: Q2.1 (G), R52.2, R53.1
- new net RLY_K: D2.2 (A), K1.8, Q2.3 (D)
- new net RX_MIX: C35.1, C36.1, R35.2, R36.2, R37.1, TP8.1
- new net SAU_3V3: C10.1, C11.1, R4.2, U3.6 (VDD)
- new net SAU_RST: R4.1, U3.9 (RSTb)
- new net SA_AUDIO_ON_n: LED6.1 (K), Q3.2 (S), R66.1, U2.1 (AUDIO_ON_n)
- new net SA_HL: Q1.3 (D), U2.7 (H/L)
- new net SA_PD: Q8.2 (S), R76.1, TP14.1, U2.6 (PD)
- new net SA_PTT_n: U13.4 (Pin_4), U2.5 (PTT_n)
- new net SA_RXD: TP12.1, U2.16 (RXD), U3.26 (TXD)
- new net SA_TXD: TP11.1, U2.17 (TXD), U3.25 (RXD)
- new net USB1_N: R13.2, R15.1, R27.1
- new net USB1_NR: R27.2, U6.3 (D-)
- new net USB1_P: R12.2, R14.1, R26.1
- new net USB1_PR: R26.2, R28.1, U6.4 (D+)
- new net USB2_N: R17.2, R19.1, U3.5 (D-)
- new net USB2_P: R16.2, R18.1, U3.4 (D+)
- new net USB3_N: J_USB3.2 (Pin_2), R21.2, R23.1
- new net USB3_P: J_USB3.3 (Pin_3), R20.2, R22.1
- new net USB_D8_P: J_HARN1.2 (Pin_2), R6.1, U5.1 (I/O1), U5.6 (I/O1)
- new net VGG_CT: C61.1, U15.3 (CT)
- new net VGG_SW: C62.1, J_VGG.1 (Pin_1), TP7.1, U15.1 (VOUT)
- new net VREF: C40.1, R38.2, R39.1, U8.3 (Pin_3), U8.5 (Pin_5)
- new net X_AMP_EN: Q9.3 (D), R79.1, U16.10 (IO0_6)
- new net X_KEY: Q6.3 (D), R73.1, U16.7 (IO0_3)
- new net X_MMUTE: R33.1, U16.11 (IO0_7)
- new net X_PA_KEY: Q7.3 (D), R75.1, U16.8 (IO0_4)
- new net X_PTT_HS1_n: Q4.3 (D), R69.1, U16.5 (IO0_1)
- new net X_PTT_HS2_n: Q5.3 (D), R71.1, U16.6 (IO0_2)
- new net X_SA_PD: Q8.3 (D), R77.1, U16.9 (IO0_5)
- new net ZEROIZE_HW: J_HARN1.14 (Pin_14), TP9.1
- no-connect marks 32 -> 39
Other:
- note added: "HARNESS, 5 V ENTRY, 3.3 V LDO, EXCITER SUPPLY"
- note added: "PTT AND EMCON LOGIC, PTT MIRROR, LEDS, EXPANDER 0x26 WITH LEVEL STAGES, TEST POINTS, FLAGS"
- note added: "SA868 EXCITER, UART BRIDGE, T/R RELAY, 10 dB PAD, LPF, PA LEADS, GATE BIAS SWITCH"
- note added: "USB AUDIO CODEC PCM2912A, HEADPHONE AMPLIFIER, MIC PREAMP, HEADSET LEADS"
- note added: "USB HUB TUSB2046B, PORT TERMINATIONS, SPARE PORT"
- note removed: "AUDIO PATHS, PTT + TR MIRROR, BRIDGE UART LINES, LED"
- note removed: "D7 CORE: RAILS, WM8960 CODEC ON I2S + I2C, 24 MHz CLOCK, PCA9555 EXPANDER 0x26, SC16IS740 UART BRIDGE 0x48"
- note removed: "DMR858M RADIO MODULE (V1.0 BOARD): CS PULL-UP AND CONTROL, KNOB CODE AND COS INTO THE EXPANDER"
- note removed: "HARNESS TO PCB-A, CELL FEED, TEST POINTS"
- note removed: "TPS61089 BOOST: CELL NODE -> 8 V / 2 A (500 kHz, ILIM 7.9 A, EN = MEZZ_EN)"
- title: MeshSat Field Kit carrier - PCB-D APRS BOARD -> MeshSat Field Kit carrier - PCB-D APRS MEZZANINE

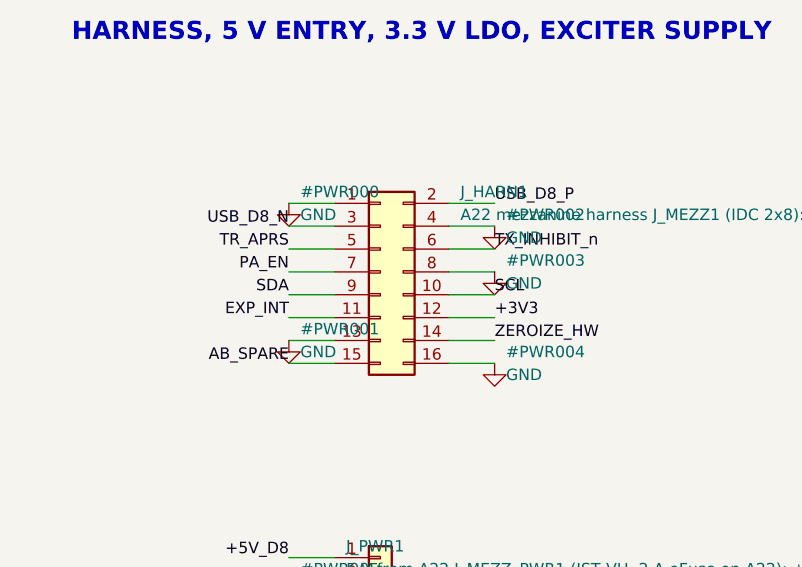
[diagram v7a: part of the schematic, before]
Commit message: test(ecad): the golden schematic test, and the six board files regenerated to match their generators [MESHSAT-862]
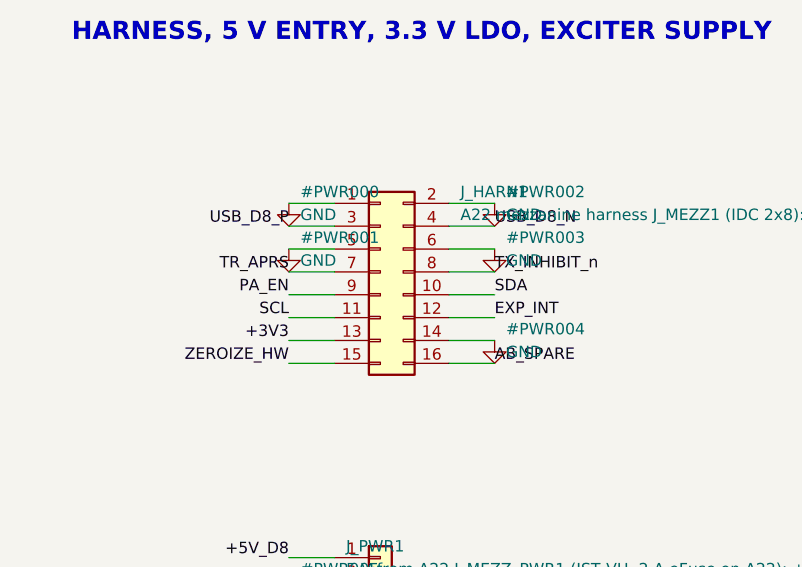
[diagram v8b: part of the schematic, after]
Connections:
- net +3V3: now also J_HARN1.13 (Pin_13); no longer J_HARN1.12 (Pin_12)
- net AB_SPARE: now also J_HARN1.16 (Pin_16); no longer J_HARN1.15 (Pin_15)
- net EXP_INT: now also J_HARN1.12 (Pin_12); no longer J_HARN1.11 (Pin_11)
- net GND: now also J_HARN1.14 (Pin_14), J_HARN1.2 (Pin_2), J_HARN1.5 (Pin_5), J_HARN1.6 (Pin_6); no longer J_HARN1.13 (Pin_13), J_HARN1.16 (Pin_16), J_HARN1.4 (Pin_4), J_HARN1.8 (Pin_8)
- net PA_EN: now also J_HARN1.9 (Pin_9); no longer J_HARN1.7 (Pin_7)
- net SCL: now also J_HARN1.11 (Pin_11); no longer J_HARN1.10 (Pin_10)
- net SDA: now also J_HARN1.10 (Pin_10); no longer J_HARN1.9 (Pin_9)
- net TR_APRS: now also J_HARN1.7 (Pin_7); no longer J_HARN1.5 (Pin_5)
- net TX_INHIBIT_n: now also J_HARN1.8 (Pin_8); no longer J_HARN1.6 (Pin_6)
- net USB_D8_N: now also J_HARN1.4 (Pin_4); no longer J_HARN1.3 (Pin_3)
- net USB_D8_P: now also J_HARN1.3 (Pin_3); no longer J_HARN1.2 (Pin_2)
- net ZEROIZE_HW: now also J_HARN1.15 (Pin_15); no longer J_HARN1.14 (Pin_14)
